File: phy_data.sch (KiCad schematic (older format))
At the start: 18 parts

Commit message: sch: Add misc doc texts
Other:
- note added: "We need to get LEDs outside of this sheet\nas they are used for config"
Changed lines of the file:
@@
 Wire Bus Line
 	4300 4400 4300 5800
+Text Notes 3250 6500 0    50   ~ 0
+We need to get LEDs outside of this sheet\nas they are used for config
 $EndSCHEMATC

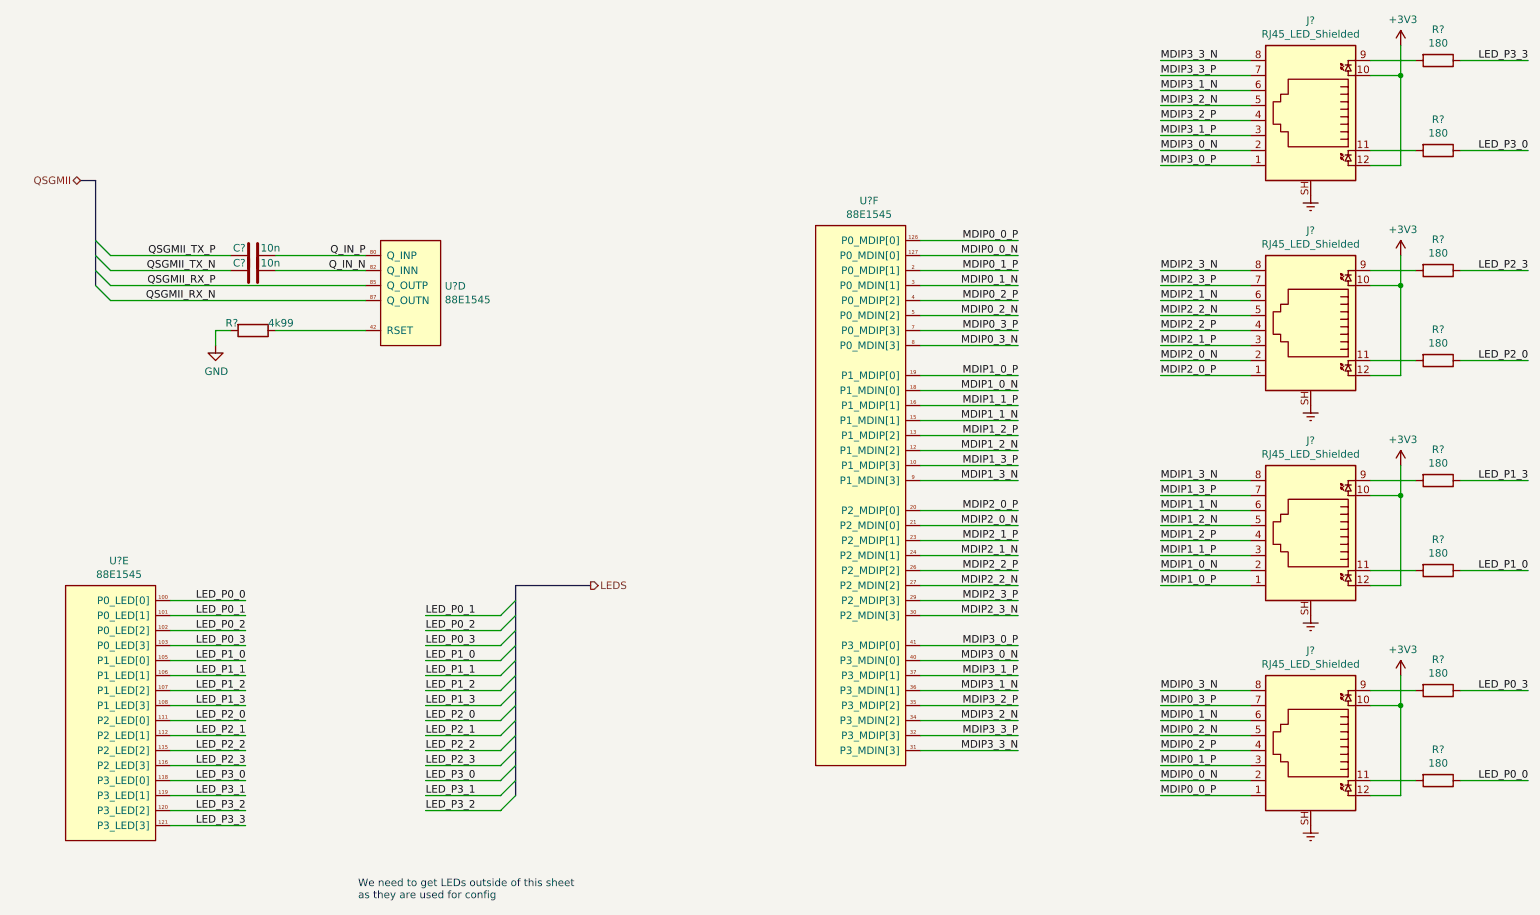
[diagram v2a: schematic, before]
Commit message: sch: Replace regular symbols with small variant
Done for most capacitors and resistors
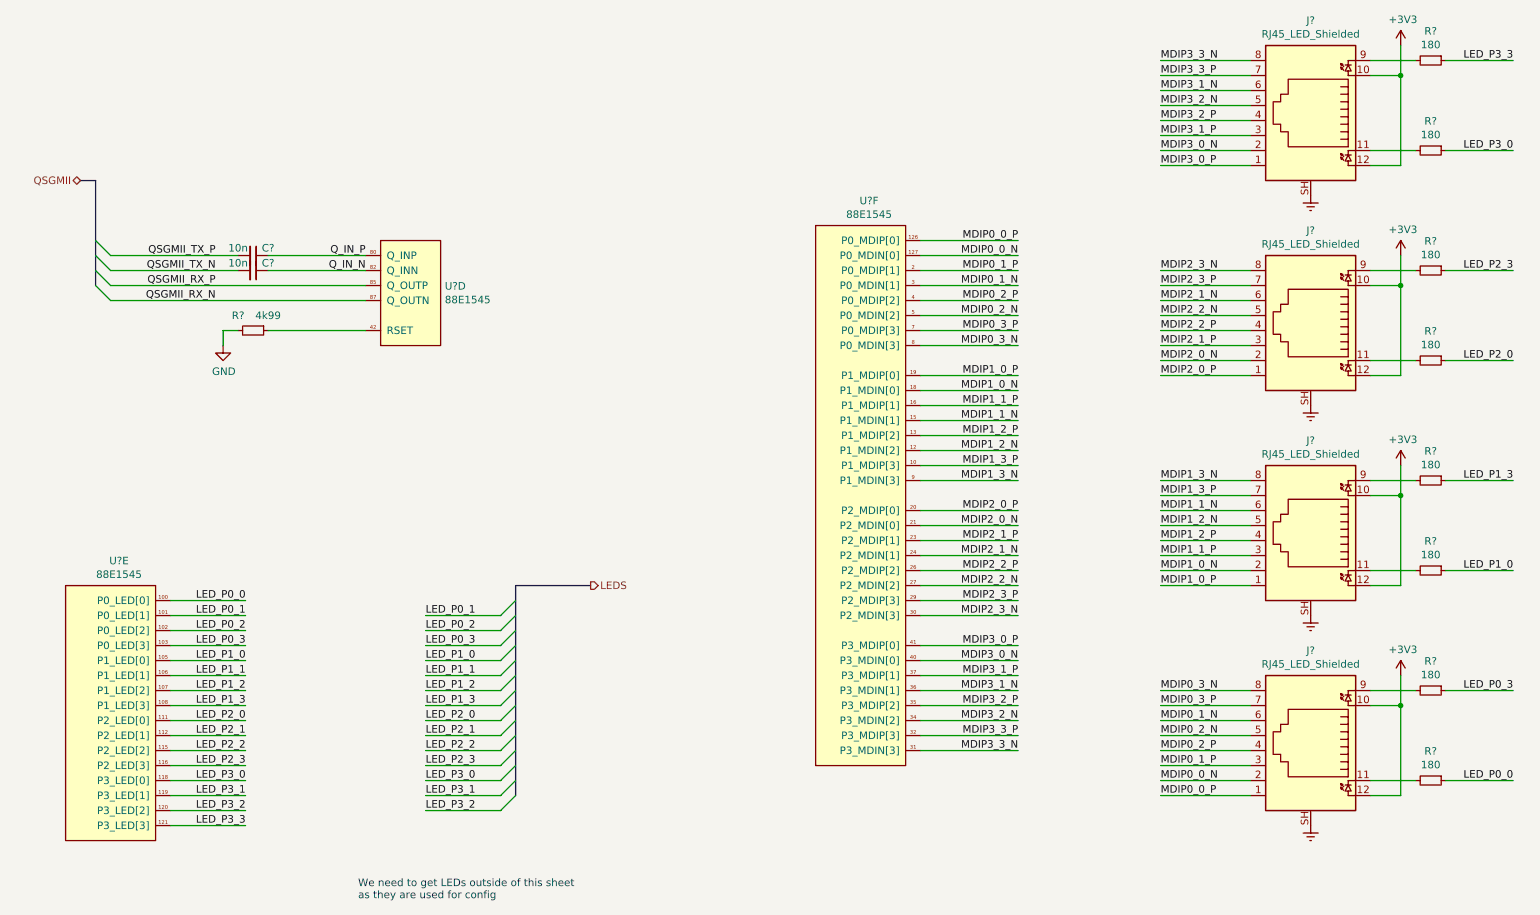
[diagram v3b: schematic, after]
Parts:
- removed C? (x2): 10n, Capacitor_SMD:C_0603_1608Metric, symbol Device:C
- removed R?: 4k99, Resistor_SMD:R_0603_1608Metric, symbol Device:R
- removed R? (x8): 180, symbol Device:R
- added C? (x2): 10n, symbol Device:C_Small
- added R? (x8): 180, symbol Device:R_Small
- added R?: 4k99, symbol Device:R_Small
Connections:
- net GND: now also R?.2
- net LED_P0_0: now also R?.1
- net LED_P0_3: now also R?.1
- net LED_P1_0: now also R?.1
- net LED_P1_3: now also R?.1
- net LED_P2_0: now also R?.1
- net LED_P2_3: now also R?.1
- net LED_P3_0: now also R?.1
- net LED_P3_3: now also R?.1
- net QSGMII_TX_N: now also C?.2
- net QSGMII_TX_P: now also C?.2
- net Q_IN_N: now also C?.1
- net Q_IN_P: now also C?.1
- net at U?.42 (RSET): now also R?.1
- net at J?.11: now also R?.2 (x4)
- net at J?.9: now also R?.2 (x4)
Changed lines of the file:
@@
 	1    0    0    -1
 $EndComp
-$Comp
-L Device:C C?
-U 1 1 5C7D6976
-P 2550 2200
-F 0 "C?" V 2500 2150 50  0000 R CNN
-F 1 "10n" V 2500 2250 50  0000 L CNN
-F 2 "Capacitor_SMD:C_0603_1608Metric" H 2588 2050 50  0001 C CNN
-F 3 "~" H 2550 2200 50  0001 C CNN
-	1    2550 2200
-	0    1    1    0
-$EndComp
-$Comp
-L Device:C C?
-U 1 1 5C7D69DD
-P 2550 2300
-F 0 "C?" V 2500 2250 50  0000 R CNN
-F 1 "10n" V 2500 2350 50  0000 L CNN
-F 2 "Capacitor_SMD:C_0603_1608Metric" H 2588 2150 50  0001 C CNN
-F 3 "~" H 2550 2300 50  0001 C CNN
-	1    2550 2300
-	0    1    1    0
-$EndComp
-Wire Wire Line
-	2700 2200 3300 2200
+Wire Wire Line
+	2650 2200 3300 2200
 Text Label 3300 2200 2    50   ~ 0
 Q_IN_P
 Wire Wire Line
-	2700 2300 3300 2300
+	2650 2300 3300 2300
 Text Label 3300 2300 2    50   ~ 0
 Q_IN_N
@@
 QSGMII_TX_P
 Wire Wire Line
-	2400 2300 1600 2300
-Wire Wire Line
-	1600 2200 2400 2200
+	2450 2300 1600 2300
+Wire Wire Line
+	1600 2200 2450 2200
 Wire Wire Line
 	1600 2400 3300 2400
@@
 QSGMII_RX_N
 $Comp
-L Device:R R?
-U 1 1 5C7D7973
-P 2550 2700
-F 0 "R?" V 2500 2600 50  0000 R CNN
-F 1 "4k99" V 2500 2800 50  0000 L CNN
-F 2 "Resistor_SMD:R_0603_1608Metric" V 2480 2700 50  0001 C CNN
-F 3 "~" H 2550 2700 50  0001 C CNN
-	1    2550 2700
-	0    1    1    0
-$EndComp
-$Comp
 L power:GND #PWR?
 U 1 1 5C7D7B57
-P 2300 2800
-F 0 "#PWR?" H 2300 2550 50  0001 C CNN
-F 1 "GND" H 2305 2627 50  0000 C CNN
-F 2 "" H 2300 2800 50  0001 C CNN
-F 3 "" H 2300 2800 50  0001 C CNN
-	1    2300 2800
-	1    0    0    -1
-$EndComp
-Wire Wire Line
-	2700 2700 3300 2700
-Wire Wire Line
-	2400 2700 2300 2700
-Wire Wire Line
-	2300 2700 2300 2800
+P 2350 2800
+F 0 "#PWR?" H 2350 2550 50  0001 C CNN
+F 1 "GND" H 2355 2627 50  0000 C CNN
+F 2 "" H 2350 2800 50  0001 C CNN
+F 3 "" H 2350 2800 50  0001 C CNN
+	1    2350 2800
+	1    0    0    -1
+$EndComp
+Wire Wire Line
+	2650 2700 3300 2700
+Wire Wire Line
+	2450 2700 2350 2700
+Wire Wire Line
+	2350 2700 2350 2800
 $Comp
 L Connector:RJ45_LED_Shielded J?
@@
 Wire Wire Line
 	10200 800  10200 1000
-$Comp
-L Device:R R?
-U 1 1 5C92A712
-P 10450 900
-F 0 "R?" V 10243 900 50  0000 C CNN
-F 1 "180" V 10334 900 50  0000 C CNN
-F 2 "" V 10380 900 50  0001 C CNN
-F 3 "~" H 10450 900 50  0001 C CNN
-	1    10450 900
-	0    1    1    0
-$EndComp
 Wire Wire Line
 	10000 900  10300 900
-$Comp
-L Device:R R?
-U 1 1 5C92F087
-P 10450 1500
-F 0 "R?" V 10243 1500 50  0000 C CNN
-F 1 "180" V 10334 1500 50  0000 C CNN
-F 2 "" V 10380 1500 50  0001 C CNN
-F 3 "~" H 10450 1500 50  0001 C CNN
-	1    10450 1500
-	0    1    1    0
-$EndComp
 Wire Wire Line
 	10000 1500 10300 1500
-Text Label 11050 900  2    50   ~ 0
+Text Label 10950 900  2    50   ~ 0
 LED_P3_3
-Text Label 11050 1500 2    50   ~ 0
+Text Label 10950 1500 2    50   ~ 0
 LED_P3_0
 Wire Wire Line
-	11050 900  10600 900
-Wire Wire Line
-	11050 1500 10600 1500
+	10950 900  10500 900
+Wire Wire Line
+	10950 1500 10500 1500
 $Comp
 L power:+3V3 #PWR?
@@
 Wire Wire Line
 	10200 2200 10200 2400
-$Comp
-L Device:R R?
-U 1 1 5C94B8BB
-P 10450 2300
-F 0 "R?" V 10243 2300 50  0000 C CNN
-F 1 "180" V 10334 2300 50  0000 C CNN
-F 2 "" V 10380 2300 50  0001 C CNN
-F 3 "~" H 10450 2300 50  0001 C CNN
-	1    10450 2300
-	0    1    1    0
-$EndComp
 Wire Wire Line
 	10000 2300 10300 2300
-$Comp
-L Device:R R?
-U 1 1 5C94B8C3
-P 10450 2900
-F 0 "R?" V 10243 2900 50  0000 C CNN
-F 1 "180" V 10334 2900 50  0000 C CNN
-F 2 "" V 10380 2900 50  0001 C CNN
-F 3 "~" H 10450 2900 50  0001 C CNN
-	1    10450 2900
-	0    1    1    0
-$EndComp
 Wire Wire Line
 	10000 2900 10300 2900
-Text Label 11050 2300 2    50   ~ 0
+Text Label 10950 2300 2    50   ~ 0
 LED_P2_3
-Text Label 11050 2900 2    50   ~ 0
+Text Label 10950 2900 2    50   ~ 0
 LED_P2_0
 Wire Wire Line
-	11050 2300 10600 2300
-Wire Wire Line
-	11050 2900 10600 2900
+	10950 2300 10500 2300
+Wire Wire Line
+	10950 2900 10500 2900
 $Comp
 L power:+3V3 #PWR?
@@
 Wire Wire Line
 	10200 3600 10200 3800
-$Comp
-L Device:R R?
-U 1 1 5C950C8D
-P 10450 3700
-F 0 "R?" V 10243 3700 50  0000 C CNN
-F 1 "180" V 10334 3700 50  0000 C CNN
-F 2 "" V 10380 3700 50  0001 C CNN
-F 3 "~" H 10450 3700 50  0001 C CNN
-	1    10450 3700
-	0    1    1    0
-$EndComp
 Wire Wire Line
 	10000 3700 10300 3700
-$Comp
-L Device:R R?
-U 1 1 5C950C95
-P 10450 4300
-F 0 "R?" V 10243 4300 50  0000 C CNN
-F 1 "180" V 10334 4300 50  0000 C CNN
-F 2 "" V 10380 4300 50  0001 C CNN
-F 3 "~" H 10450 4300 50  0001 C CNN
-	1    10450 4300
-	0    1    1    0
-$EndComp
 Wire Wire Line
 	10000 4300 10300 4300
-Text Label 11050 3700 2    50   ~ 0
+Text Label 10950 3700 2    50   ~ 0
 LED_P1_3
-Text Label 11050 4300 2    50   ~ 0
+Text Label 10950 4300 2    50   ~ 0
 LED_P1_0
 Wire Wire Line
-	11050 3700 10600 3700
-Wire Wire Line
-	11050 4300 10600 4300
+	10950 3700 10500 3700
+Wire Wire Line
+	10950 4300 10500 4300
 $Comp
 L power:+3V3 #PWR?
@@
 Wire Wire Line
 	10200 5000 10200 5200
-$Comp
-L Device:R R?
-U 1 1 5C9567C8
-P 10450 5100
-F 0 "R?" V 10243 5100 50  0000 C CNN
-F 1 "180" V 10334 5100 50  0000 C CNN
-F 2 "" V 10380 5100 50  0001 C CNN
-F 3 "~" H 10450 5100 50  0001 C CNN
-	1    10450 5100
-	0    1    1    0
-$EndComp
 Wire Wire Line
 	10000 5100 10300 5100
-$Comp
-L Device:R R?
-U 1 1 5C9567D0
-P 10450 5700
-F 0 "R?" V 10243 5700 50  0000 C CNN
-F 1 "180" V 10334 5700 50  0000 C CNN
-F 2 "" V 10380 5700 50  0001 C CNN
-F 3 "~" H 10450 5700 50  0001 C CNN
-	1    10450 5700
-	0    1    1    0
-$EndComp
 Wire Wire Line
 	10000 5700 10300 5700
-Text Label 11050 5100 2    50   ~ 0
+Text Label 10950 5100 2    50   ~ 0
 LED_P0_3
-Text Label 11050 5700 2    50   ~ 0
+Text Label 10950 5700 2    50   ~ 0
 LED_P0_0
 Wire Wire Line
-	11050 5100 10600 5100
-Wire Wire Line
-	11050 5700 10600 5700
+	10950 5100 10500 5100
+Wire Wire Line
+	10950 5700 10500 5700
 $Comp
 L power:Earth #PWR?
@@
 Entry Wire Line
 	1500 2200 1600 2300
+Text Notes 3250 6500 0    50   ~ 0
+We need to get LEDs outside of this sheet\nas they are used for config
+$Comp
+L Device:R_Small R?
+U 1 1 5D4C05CB
+P 10400 900
+F 0 "R?" V 10204 900 50  0000 C CNN
+F 1 "180" V 10295 900 50  0000 C CNN
+F 2 "" H 10400 900 50  0001 C CNN
+F 3 "~" H 10400 900 50  0001 C CNN
+	1    10400 900
+	0    1    1    0
+$EndComp
+$Comp
+L Device:R_Small R?
+U 1 1 5D4D2934
+P 10400 1500
+F 0 "R?" V 10204 1500 50  0000 C CNN
+F 1 "180" V 10295 1500 50  0000 C CNN
+F 2 "" H 10400 1500 50  0001 C CNN
+F 3 "~" H 10400 1500 50  0001 C CNN
+	1    10400 1500
+	0    1    1    0
+$EndComp
+$Comp
+L Device:R_Small R?
+U 1 1 5D4DBDE3
+P 10400 2300
+F 0 "R?" V 10204 2300 50  0000 C CNN
+F 1 "180" V 10295 2300 50  0000 C CNN
+F 2 "" H 10400 2300 50  0001 C CNN
+F 3 "~" H 10400 2300 50  0001 C CNN
+	1    10400 2300
+	0    1    1    0
+$EndComp
+$Comp
+L Device:R_Small R?
+U 1 1 5D4DBDE9
+P 10400 2900
+F 0 "R?" V 10204 2900 50  0000 C CNN
+F 1 "180" V 10295 2900 50  0000 C CNN
+F 2 "" H 10400 2900 50  0001 C CNN
+F 3 "~" H 10400 2900 50  0001 C CNN
+	1    10400 2900
+	0    1    1    0
+$EndComp
+$Comp
+L Device:R_Small R?
+U 1 1 5D4E554E
+P 10400 3700
+F 0 "R?" V 10204 3700 50  0000 C CNN
+F 1 "180" V 10295 3700 50  0000 C CNN
+F 2 "" H 10400 3700 50  0001 C CNN
+F 3 "~" H 10400 3700 50  0001 C CNN
+	1    10400 3700
+	0    1    1    0
+$EndComp
+$Comp
+L Device:R_Small R?
+U 1 1 5D4E5554
+P 10400 4300
+F 0 "R?" V 10204 4300 50  0000 C CNN
+F 1 "180" V 10295 4300 50  0000 C CNN
+F 2 "" H 10400 4300 50  0001 C CNN
+F 3 "~" H 10400 4300 50  0001 C CNN
+	1    10400 4300
+	0    1    1    0
+$EndComp
+$Comp
+L Device:R_Small R?
+U 1 1 5D4E555A
+P 10400 5100
+F 0 "R?" V 10204 5100 50  0000 C CNN
+F 1 "180" V 10295 5100 50  0000 C CNN
+F 2 "" H 10400 5100 50  0001 C CNN
+F 3 "~" H 10400 5100 50  0001 C CNN
+	1    10400 5100
+	0    1    1    0
+$EndComp
+$Comp
+L Device:R_Small R?
+U 1 1 5D4E5560
+P 10400 5700
+F 0 "R?" V 10204 5700 50  0000 C CNN
+F 1 "180" V 10295 5700 50  0000 C CNN
+F 2 "" H 10400 5700 50  0001 C CNN
+F 3 "~" H 10400 5700 50  0001 C CNN
+	1    10400 5700
+	0    1    1    0
+$EndComp
+$Comp
+L Device:R_Small R?
+U 1 1 5D4F6574
+P 2550 2700
+F 0 "R?" V 2450 2600 50  0000 C CNN
+F 1 "4k99" V 2450 2800 50  0000 C CNN
+F 2 "" H 2550 2700 50  0001 C CNN
+F 3 "~" H 2550 2700 50  0001 C CNN
+	1    2550 2700
+	0    1    1    0
+$EndComp
+$Comp
+L Device:C_Small C?
+U 1 1 5D513AC6
+P 2550 2200
+F 0 "C?" V 2500 2300 50  0000 C CNN
+F 1 "10n" V 2500 2100 50  0000 C CNN
+F 2 "" H 2550 2200 50  0001 C CNN
+F 3 "~" H 2550 2200 50  0001 C CNN
+	1    2550 2200
+	0    1    1    0
+$EndComp
+$Comp
+L Device:C_Small C?
+U 1 1 5D516975
+P 2550 2300
+F 0 "C?" V 2500 2400 50  0000 C CNN
+F 1 "10n" V 2500 2200 50  0000 C CNN
+F 2 "" H 2550 2300 50  0001 C CNN
+F 3 "~" H 2550 2300 50  0001 C CNN
+	1    2550 2300
+	0    1    1    0
+$EndComp
 Wire Bus Line
 	1500 1700 1500 2400
 Wire Bus Line
 	4300 4400 4300 5800
-Text Notes 3250 6500 0    50   ~ 0
-We need to get LEDs outside of this sheet\nas they are used for config
 $EndSCHEMATC
